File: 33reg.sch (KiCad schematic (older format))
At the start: 0 parts

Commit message: add reg ic + circuit
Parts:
- added C? (x2): C, ~, symbol C
- added L?: INDUCTOR, ~, symbol INDUCTOR
- added P? (x3): TST, ~, symbol TST
- added U?: AAT1110IJS-3.3-T1, symbol AAT1110IJS-3.3-T1
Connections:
- new net: L?.2, U?.4 (LX)
- new net +3.3v: C?.2, L?.1, P?.1, U?.2 (OUT)
- new net +5v: C?.1, P?.1, U?.1 (EN), U?.3 (VIN)
- new net GND: C?.1, C?.2, P?.1, U?.5 (AGND), U?.6 (PGND), U?.7 (PGND), U?.8 (PGND)
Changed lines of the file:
@@
-EESchema Schematic File Version 2  date 10/14/2013 7:57:20 AM
+EESchema Schematic File Version 2  date 10/14/2013 8:27:34 AM
 LIBS:power
 LIBS:device
@@
 LIBS:contrib
 LIBS:valves
+LIBS:kicadlib
 EELAYER 27 0
 EELAYER END
@@
 Comment4 ""
 $EndDescr
+Text GLabel 3400 3200 0    60   Input ~ 0
++5v
+Text GLabel 3900 4450 0    60   Input ~ 0
++3.3v
+$Comp
+L AAT1110IJS-3.3-T1 U?
+U 1 1 525BE285
+P 4900 3450
+F 0 "U?" H 4900 3100 60  0000 C CNN
+F 1 "AAT1110IJS-3.3-T1" H 4900 3850 60  0000 C CNN
+F 2 "" H 4900 3350 60  0000 C CNN
+F 3 "" H 4900 3350 60  0000 C CNN
+	1    4900 3450
+	1    0    0    -1
+$EndComp
+Wire Wire Line
+	3400 3200 4300 3200
+Wire Wire Line
+	4300 3500 3900 3500
+Wire Wire Line
+	3900 3500 3900 3200
+Connection ~ 3900 3200
+$Comp
+L C C?
+U 1 1 525BE299
+P 3600 3550
+F 0 "C?" H 3600 3650 40  0000 L CNN
+F 1 "C" H 3606 3465 40  0000 L CNN
+F 2 "~" H 3638 3400 30  0000 C CNN
+F 3 "~" H 3600 3550 60  0000 C CNN
+	1    3600 3550
+	1    0    0    -1
+$EndComp
+Wire Wire Line
+	3600 3200 3600 3350
+Connection ~ 3600 3200
+$Comp
+L GND #PWR?
+U 1 1 525BE2C6
+P 3600 3900
+F 0 "#PWR?" H 3600 3900 30  0001 C CNN
+F 1 "GND" H 3600 3830 30  0001 C CNN
+F 2 "" H 3600 3900 60  0000 C CNN
+F 3 "" H 3600 3900 60  0000 C CNN
+	1    3600 3900
+	1    0    0    -1
+$EndComp
+$Comp
+L GND #PWR?
+U 1 1 525BE2DA
+P 5700 3850
+F 0 "#PWR?" H 5700 3850 30  0001 C CNN
+F 1 "GND" H 5700 3780 30  0001 C CNN
+F 2 "" H 5700 3850 60  0000 C CNN
+F 3 "" H 5700 3850 60  0000 C CNN
+	1    5700 3850
+	1    0    0    -1
+$EndComp
+Wire Wire Line
+	5700 3650 5500 3650
+Wire Wire Line
+	5700 3200 5700 3850
+Wire Wire Line
+	5500 3350 5700 3350
+Connection ~ 5700 3650
+Wire Wire Line
+	5500 3500 5700 3500
+Connection ~ 5700 3500
+Wire Wire Line
+	5500 3200 5700 3200
+Connection ~ 5700 3350
+$Comp
+L C C?
+U 1 1 525BE30C
+P 4150 4800
+F 0 "C?" H 4150 4900 40  0000 L CNN
+F 1 "C" H 4156 4715 40  0000 L CNN
+F 2 "~" H 4188 4650 30  0000 C CNN
+F 3 "~" H 4150 4800 60  0000 C CNN
+	1    4150 4800
+	-1   0    0    1
+$EndComp
+Wire Wire Line
+	4300 3350 4050 3350
+Wire Wire Line
+	4050 3350 4050 4450
+Wire Wire Line
+	3600 3750 3600 3900
+$Comp
+L INDUCTOR L?
+U 1 1 525BE371
+P 4300 4150
+F 0 "L?" V 4250 4150 40  0000 C CNN
+F 1 "INDUCTOR" V 4400 4150 40  0000 C CNN
+F 2 "~" H 4300 4150 60  0000 C CNN
+F 3 "~" H 4300 4150 60  0000 C CNN
+	1    4300 4150
+	-1   0    0    1
+$EndComp
+Wire Wire Line
+	4300 3650 4300 3850
+Connection ~ 4300 4450
+Connection ~ 4050 4450
+Wire Wire Line
+	3900 4450 4300 4450
+Wire Wire Line
+	4150 4600 4150 4450
+Connection ~ 4150 4450
+$Comp
+L GND #PWR?
+U 1 1 525BE457
+P 4150 5150
+F 0 "#PWR?" H 4150 5150 30  0001 C CNN
+F 1 "GND" H 4150 5080 30  0001 C CNN
+F 2 "" H 4150 5150 60  0000 C CNN
+F 3 "" H 4150 5150 60  0000 C CNN
+	1    4150 5150
+	1    0    0    -1
+$EndComp
+Wire Wire Line
+	4150 5000 4150 5150
+$Comp
+L TST P?
+U 1 1 525BE4FA
+P 5550 4700
+F 0 "P?" H 5550 5000 40  0000 C CNN
+F 1 "TST" H 5550 4950 30  0000 C CNN
+F 2 "~" H 5550 4700 60  0000 C CNN
+F 3 "~" H 5550 4700 60  0000 C CNN
+	1    5550 4700
+	1    0    0    -1
+$EndComp
+$Comp
+L TST P?
+U 1 1 525BE511
+P 5300 4700
+F 0 "P?" H 5300 5000 40  0000 C CNN
+F 1 "TST" H 5300 4950 30  0000 C CNN
+F 2 "~" H 5300 4700 60  0000 C CNN
+F 3 "~" H 5300 4700 60  0000 C CNN
+	1    5300 4700
+	1    0    0    -1
+$EndComp
+$Comp
+L TST P?
+U 1 1 525BE517
+P 5050 4700
+F 0 "P?" H 5050 5000 40  0000 C CNN
+F 1 "TST" H 5050 4950 30  0000 C CNN
+F 2 "~" H 5050 4700 60  0000 C CNN
+F 3 "~" H 5050 4700 60  0000 C CNN
+	1    5050 4700
+	1    0    0    -1
+$EndComp
+Text GLabel 5050 4850 3    60   Input ~ 0
++5v
+Text GLabel 5550 4850 3    60   Input ~ 0
++3.3v
+$Comp
+L GND #PWR?
+U 1 1 525BE51F
+P 5300 4850
+F 0 "#PWR?" H 5300 4850 30  0001 C CNN
+F 1 "GND" H 5300 4780 30  0001 C CNN
+F 2 "" H 5300 4850 60  0000 C CNN
+F 3 "" H 5300 4850 60  0000 C CNN
+	1    5300 4850
+	1    0    0    -1
+$EndComp
+Wire Wire Line
+	5050 4700 5050 4850
+Wire Wire Line
+	5300 4850 5300 4700
+Wire Wire Line
+	5550 4700 5550 4850
 $EndSCHEMATC

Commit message: annotate and netlist
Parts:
- gave numbers to parts that had none: 7
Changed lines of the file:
@@
-EESchema Schematic File Version 2  date 10/14/2013 8:27:34 AM
+EESchema Schematic File Version 2  date 10/14/2013 8:28:50 AM
 LIBS:power
 LIBS:device
@@
 LIBS:valves
 LIBS:kicadlib
+LIBS:33reg-cache
 EELAYER 27 0
 EELAYER END
@@
 +3.3v
 $Comp
-L AAT1110IJS-3.3-T1 U?
+L AAT1110IJS-3.3-T1 U1
 U 1 1 525BE285
 P 4900 3450
-F 0 "U?" H 4900 3100 60  0000 C CNN
+F 0 "U1" H 4900 3100 60  0000 C CNN
 F 1 "AAT1110IJS-3.3-T1" H 4900 3850 60  0000 C CNN
 F 2 "" H 4900 3350 60  0000 C CNN
@@
 Connection ~ 3900 3200
 $Comp
-L C C?
+L C C1
 U 1 1 525BE299
 P 3600 3550
-F 0 "C?" H 3600 3650 40  0000 L CNN
+F 0 "C1" H 3600 3650 40  0000 L CNN
 F 1 "C" H 3606 3465 40  0000 L CNN
 F 2 "~" H 3638 3400 30  0000 C CNN
@@
 Connection ~ 3600 3200
 $Comp
-L GND #PWR?
+L GND #PWR01
 U 1 1 525BE2C6
 P 3600 3900
-F 0 "#PWR?" H 3600 3900 30  0001 C CNN
+F 0 "#PWR01" H 3600 3900 30  0001 C CNN
 F 1 "GND" H 3600 3830 30  0001 C CNN
 F 2 "" H 3600 3900 60  0000 C CNN
@@
 $EndComp
 $Comp
-L GND #PWR?
+L GND #PWR02
 U 1 1 525BE2DA
 P 5700 3850
-F 0 "#PWR?" H 5700 3850 30  0001 C CNN
+F 0 "#PWR02" H 5700 3850 30  0001 C CNN
 F 1 "GND" H 5700 3780 30  0001 C CNN
 F 2 "" H 5700 3850 60  0000 C CNN
@@
 Connection ~ 5700 3350
 $Comp
-L C C?
+L C C2
 U 1 1 525BE30C
 P 4150 4800
-F 0 "C?" H 4150 4900 40  0000 L CNN
+F 0 "C2" H 4150 4900 40  0000 L CNN
 F 1 "C" H 4156 4715 40  0000 L CNN
 F 2 "~" H 4188 4650 30  0000 C CNN
@@
 	3600 3750 3600 3900
 $Comp
-L INDUCTOR L?
+L INDUCTOR L1
 U 1 1 525BE371
 P 4300 4150
-F 0 "L?" V 4250 4150 40  0000 C CNN
+F 0 "L1" V 4250 4150 40  0000 C CNN
 F 1 "INDUCTOR" V 4400 4150 40  0000 C CNN
 F 2 "~" H 4300 4150 60  0000 C CNN
@@
 Connection ~ 4150 4450
 $Comp
-L GND #PWR?
+L GND #PWR03
 U 1 1 525BE457
 P 4150 5150
-F 0 "#PWR?" H 4150 5150 30  0001 C CNN
+F 0 "#PWR03" H 4150 5150 30  0001 C CNN
 F 1 "GND" H 4150 5080 30  0001 C CNN
 F 2 "" H 4150 5150 60  0000 C CNN
@@
 	4150 5000 4150 5150
 $Comp
-L TST P?
+L TST P3
 U 1 1 525BE4FA
 P 5550 4700
-F 0 "P?" H 5550 5000 40  0000 C CNN
+F 0 "P3" H 5550 5000 40  0000 C CNN
 F 1 "TST" H 5550 4950 30  0000 C CNN
 F 2 "~" H 5550 4700 60  0000 C CNN
@@
 $EndComp
 $Comp
-L TST P?
+L TST P2
 U 1 1 525BE511
 P 5300 4700
-F 0 "P?" H 5300 5000 40  0000 C CNN
+F 0 "P2" H 5300 5000 40  0000 C CNN
 F 1 "TST" H 5300 4950 30  0000 C CNN
 F 2 "~" H 5300 4700 60  0000 C CNN
@@
 $EndComp
 $Comp
-L TST P?
+L TST P1
 U 1 1 525BE517
 P 5050 4700
-F 0 "P?" H 5050 5000 40  0000 C CNN
+F 0 "P1" H 5050 5000 40  0000 C CNN
 F 1 "TST" H 5050 4950 30  0000 C CNN
 F 2 "~" H 5050 4700 60  0000 C CNN
@@
 +3.3v
 $Comp
-L GND #PWR?
+L GND #PWR04
 U 1 1 525BE51F
 P 5300 4850
-F 0 "#PWR?" H 5300 4850 30  0001 C CNN
+F 0 "#PWR04" H 5300 4850 30  0001 C CNN
 F 1 "GND" H 5300 4780 30  0001 C CNN
 F 2 "" H 5300 4850 60  0000 C CNN

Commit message: start pcb
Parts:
- added P4: TST, ~, symbol TST
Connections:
- net GND: now also P4.1
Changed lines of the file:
@@
-EESchema Schematic File Version 2  date 10/14/2013 8:28:50 AM
+EESchema Schematic File Version 2  date 10/14/2013 9:11:53 AM
 LIBS:power
 LIBS:device
@@
 Wire Wire Line
 	5550 4700 5550 4850
+$Comp
+L TST P4
+U 1 1 525BEDCA
+P 5800 4700
+F 0 "P4" H 5800 5000 40  0000 C CNN
+F 1 "TST" H 5800 4950 30  0000 C CNN
+F 2 "~" H 5800 4700 60  0000 C CNN
+F 3 "~" H 5800 4700 60  0000 C CNN
+	1    5800 4700
+	1    0    0    -1
+$EndComp
+$Comp
+L GND #PWR05
+U 1 1 525BEDD0
+P 5800 4850
+F 0 "#PWR05" H 5800 4850 30  0001 C CNN
+F 1 "GND" H 5800 4780 30  0001 C CNN
+F 2 "" H 5800 4850 60  0000 C CNN
+F 3 "" H 5800 4850 60  0000 C CNN
+	1    5800 4850
+	1    0    0    -1
+$EndComp
+Wire Wire Line
+	5800 4850 5800 4700
 $EndSCHEMATC

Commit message: - add values for caps
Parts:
- C1: value C -> 4.7uF
- C2: value C -> 22uF
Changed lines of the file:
@@
-EESchema Schematic File Version 2  date 10/14/2013 9:11:53 AM
+EESchema Schematic File Version 2
 LIBS:power
 LIBS:device
@@
 Sheet 1 1
 Title ""
-Date "14 oct 2013"
+Date "7 nov 2013"
 Rev ""
 Comp ""
@@
 P 3600 3550
 F 0 "C1" H 3600 3650 40  0000 L CNN
-F 1 "C" H 3606 3465 40  0000 L CNN
+F 1 "4.7uF" H 3606 3465 40  0000 L CNN
 F 2 "~" H 3638 3400 30  0000 C CNN
 F 3 "~" H 3600 3550 60  0000 C CNN
@@
 P 4150 4800
 F 0 "C2" H 4150 4900 40  0000 L CNN
-F 1 "C" H 4156 4715 40  0000 L CNN
+F 1 "22uF" H 4156 4715 40  0000 L CNN
 F 2 "~" H 4188 4650 30  0000 C CNN
 F 3 "~" H 4150 4800 60  0000 C CNN

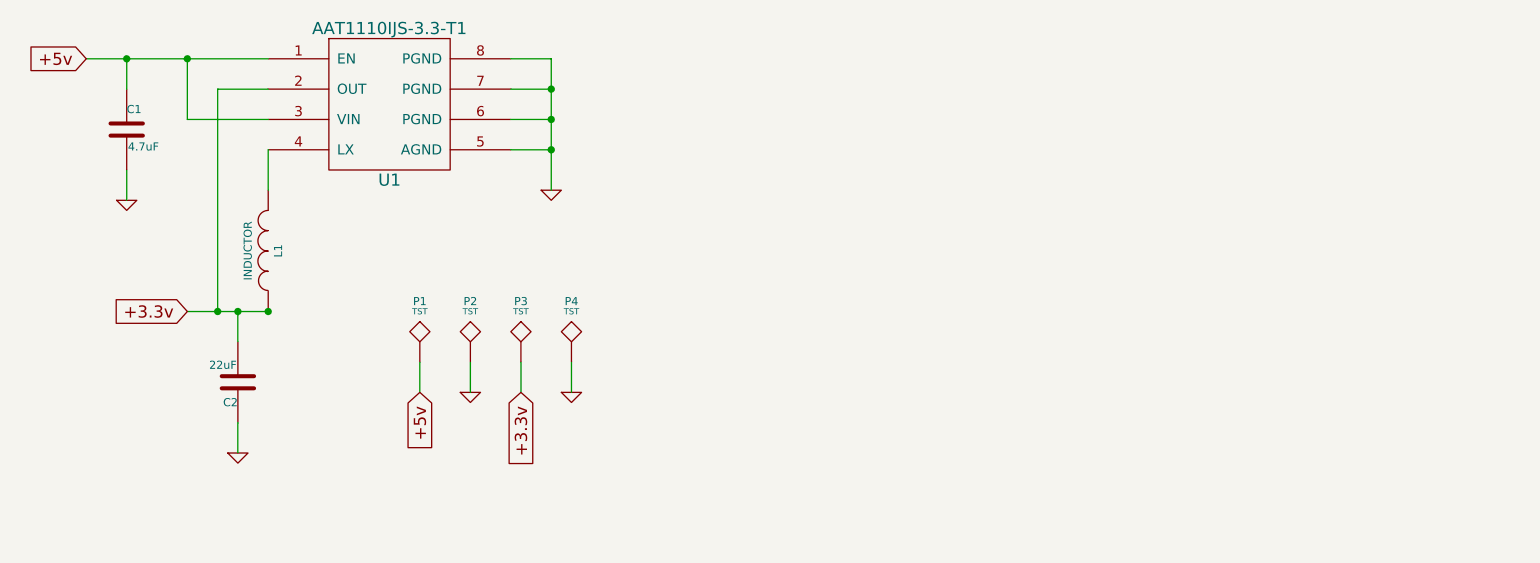
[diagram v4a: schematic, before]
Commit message: - add sample 4 switch buck-boost circuit
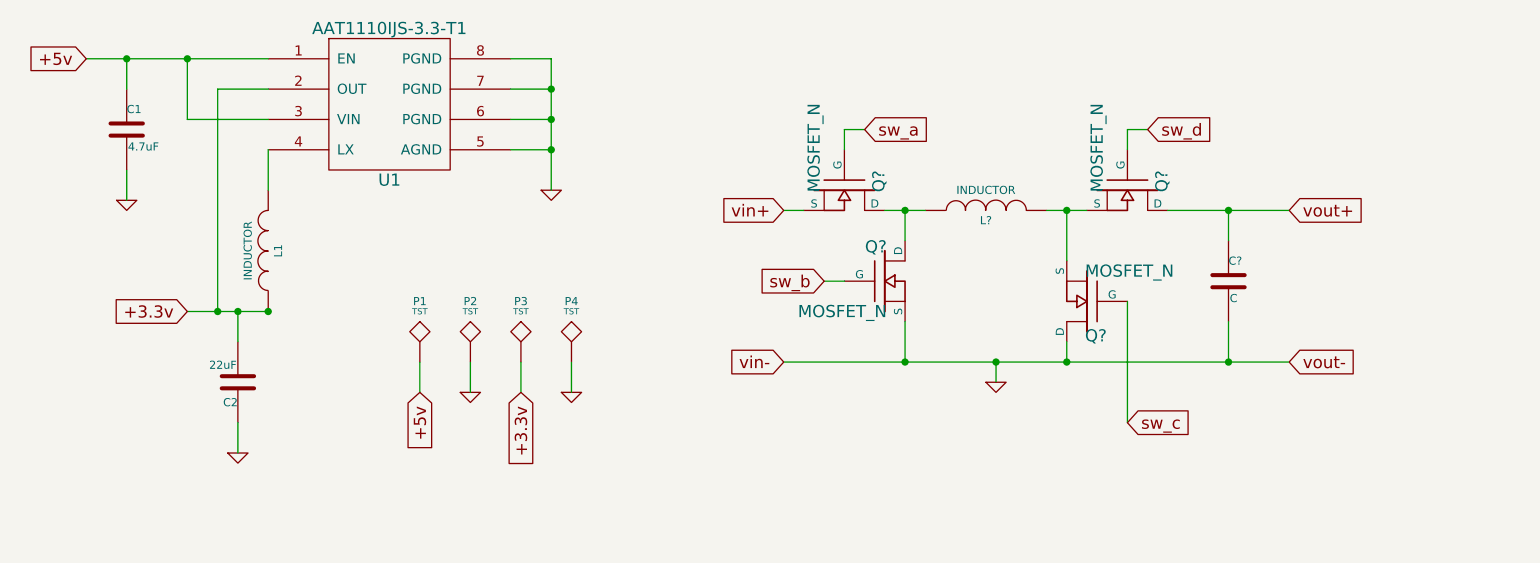
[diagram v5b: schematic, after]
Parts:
- added C?: C, ~, symbol C
- added L?: INDUCTOR, ~, symbol INDUCTOR
- added Q? (x4): MOSFET_N, ~, symbol MOSFET_N
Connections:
- net GND: now also C?.2, Q?.D, Q?.S
- new net: L?.1, Q?.D, Q?.D
- new net: L?.2, Q?.S, Q?.S
- new net sw_a: Q?.G
- new net sw_b: Q?.G
- new net sw_c: Q?.G
- new net sw_d: Q?.G
- new net vin+: Q?.S
- new net vout+: C?.1, Q?.D
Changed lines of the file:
@@
 Wire Wire Line
 	5800 4850 5800 4700
+$Comp
+L INDUCTOR L?
+U 1 1 527BCEFC
+P 7850 3950
+F 0 "L?" V 7800 3950 40  0000 C CNN
+F 1 "INDUCTOR" V 7950 3950 40  0000 C CNN
+F 2 "~" H 7850 3950 60  0000 C CNN
+F 3 "~" H 7850 3950 60  0000 C CNN
+	1    7850 3950
+	0    -1   -1   0
+$EndComp
+Text GLabel 9350 3950 2    60   Input ~ 0
+vout+
+Text GLabel 6850 3950 0    60   Input ~ 0
+vin+
+$Comp
+L MOSFET_N Q?
+U 1 1 527BCF75
+P 7150 3850
+F 0 "Q?" H 7160 4020 60  0000 R CNN
+F 1 "MOSFET_N" H 7160 3700 60  0000 R CNN
+F 2 "~" H 7150 3850 60  0000 C CNN
+F 3 "~" H 7150 3850 60  0000 C CNN
+	1    7150 3850
+	0    1    1    0
+$EndComp
+$Comp
+L MOSFET_N Q?
+U 1 1 527BCF8C
+P 8350 4400
+F 0 "Q?" H 8360 4570 60  0000 R CNN
+F 1 "MOSFET_N" H 8360 4250 60  0000 R CNN
+F 2 "~" H 8350 4400 60  0000 C CNN
+F 3 "~" H 8350 4400 60  0000 C CNN
+	1    8350 4400
+	-1   0    0    1
+$EndComp
+Wire Wire Line
+	6850 3950 6950 3950
+Wire Wire Line
+	7350 3950 7550 3950
+Connection ~ 7450 3950
+Wire Wire Line
+	8150 3950 8350 3950
+Wire Wire Line
+	8250 3950 8250 4200
+Connection ~ 8250 3950
+$Comp
+L GND #PWR?
+U 1 1 527BD033
+P 7900 4800
+F 0 "#PWR?" H 7900 4800 30  0001 C CNN
+F 1 "GND" H 7900 4730 30  0001 C CNN
+F 2 "" H 7900 4800 60  0000 C CNN
+F 3 "" H 7900 4800 60  0000 C CNN
+	1    7900 4800
+	1    0    0    -1
+$EndComp
+Wire Wire Line
+	8250 4700 8250 4600
+Wire Wire Line
+	6850 4700 9350 4700
+Connection ~ 7900 4700
+Wire Wire Line
+	7900 4700 7900 4800
+Wire Wire Line
+	8750 3950 9350 3950
+Text GLabel 7250 3550 2    60   Input ~ 0
+sw_a
+Text GLabel 8550 5000 2    60   Input ~ 0
+sw_c
+Wire Wire Line
+	7250 3550 7150 3550
+Wire Wire Line
+	7150 3550 7150 3650
+Wire Wire Line
+	8550 5000 8550 4400
+Text GLabel 6850 4700 0    60   Input ~ 0
+vin-
+Connection ~ 7450 4700
+Text GLabel 9350 4700 2    60   Input ~ 0
+vout-
+Connection ~ 8250 4700
+$Comp
+L C C?
+U 1 1 527BD302
+P 9050 4300
+F 0 "C?" H 9050 4400 40  0000 L CNN
+F 1 "C" H 9056 4215 40  0000 L CNN
+F 2 "~" H 9088 4150 30  0000 C CNN
+F 3 "~" H 9050 4300 60  0000 C CNN
+	1    9050 4300
+	1    0    0    -1
+$EndComp
+Wire Wire Line
+	9050 4100 9050 3950
+Connection ~ 9050 3950
+Wire Wire Line
+	9050 4500 9050 4700
+Connection ~ 9050 4700
+$Comp
+L MOSFET_N Q?
+U 1 1 527BD436
+P 7350 4300
+F 0 "Q?" H 7360 4470 60  0000 R CNN
+F 1 "MOSFET_N" H 7360 4150 60  0000 R CNN
+F 2 "~" H 7350 4300 60  0000 C CNN
+F 3 "~" H 7350 4300 60  0000 C CNN
+	1    7350 4300
+	1    0    0    -1
+$EndComp
+Wire Wire Line
+	7450 4100 7450 3950
+Wire Wire Line
+	7450 4500 7450 4700
+Text GLabel 7050 4300 0    60   Input ~ 0
+sw_b
+Wire Wire Line
+	7050 4300 7150 4300
+$Comp
+L MOSFET_N Q?
+U 1 1 527BD4D8
+P 8550 3850
+F 0 "Q?" H 8560 4020 60  0000 R CNN
+F 1 "MOSFET_N" H 8560 3700 60  0000 R CNN
+F 2 "~" H 8550 3850 60  0000 C CNN
+F 3 "~" H 8550 3850 60  0000 C CNN
+	1    8550 3850
+	0    1    1    0
+$EndComp
+Text GLabel 8650 3550 2    60   Input ~ 0
+sw_d
+Wire Wire Line
+	8650 3550 8550 3550
+Wire Wire Line
+	8550 3550 8550 3650
 $EndSCHEMATC
